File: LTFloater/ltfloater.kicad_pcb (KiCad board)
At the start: 2 copper layers, 97 parts, among them J1 USB_C_Receptacle, J2 USB_C_Receptacle, J3 TC2030-IDC, J4 D4, J5 D5, J6 A6, J7 A7, J8 B0, K0 K00, K1 K01, K10 K10, K11 K11, K12 K12, K13 K13, K14 K14, K14b1 K14, K2 K02, K20 K20, K21 K21, K22 K22, K23 K23, K24 K24, K3 K03, K30 K30, K31 K31, K31b1 K31, K32 K32, K33 K33, K34 K34, K34b1 K34, K4 K04, SW1 Switch-6P-2S2T, SW2 SW_Push, U1 MCP73831, U2 MCP1700 (3.0V), U3 MCP1700 (3.3V), U4 ATXMEGA-A4U-EPAD, U6 nRF24L01_module, U7 FSUSB42, U8 FSUSB42, U9 FSUSB42

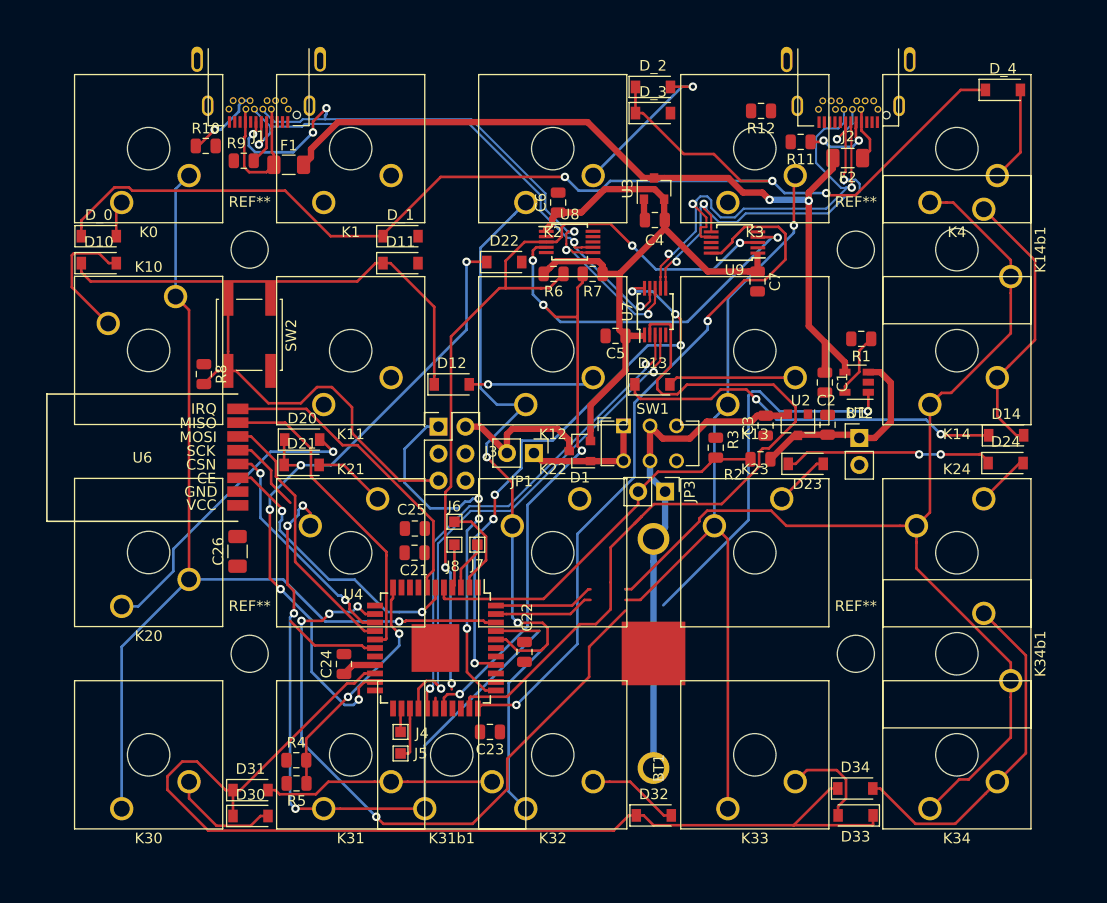
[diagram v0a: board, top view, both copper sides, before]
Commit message: Complete PCB, DRC violations limited to USB-C
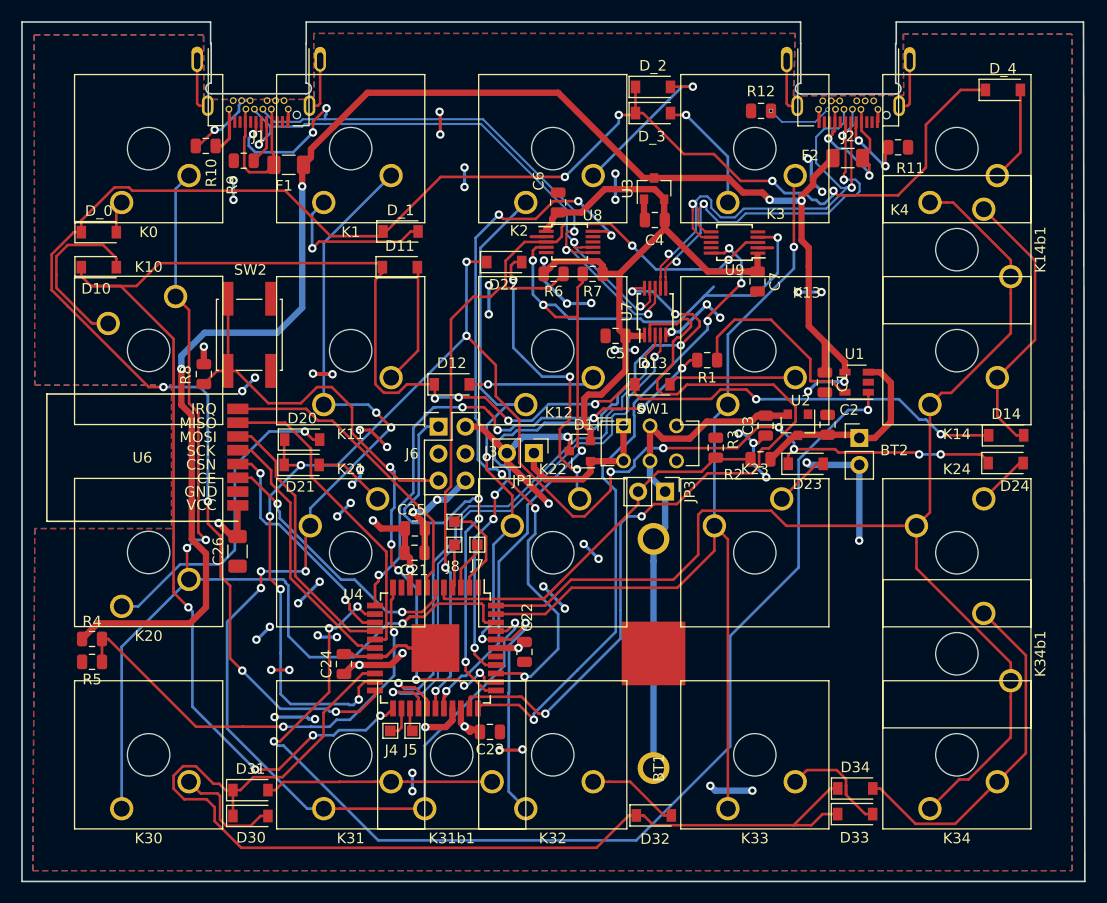
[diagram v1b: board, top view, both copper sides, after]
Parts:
- removed REF** (x4): MountingHole_3.5mm, MountingHole:MountingHole_3.5mm
- J1, J2: footprint Extra:USB_C_Receptacle_JAE_DX07B024XJ1 -> Extra:USB_C_Receptacle_JAE_DX07B024XJ1_cuts
- moved R5 22.4 mm to (98.2, 102.4)
- moved R4 22.4 mm to (98.2, 100.2)
- moved R1 14.7 mm to (156.2, 73.9)
- moved R11 9.21 mm to (174.2, 53.8), turned to 0 degrees
- moved J5 2.41 mm to (128.4, 108.9)
- moved J4 0.97 mm to (126.3, 108.9)
- moved D_1 0.44 mm to (127.3, 61.8)
- moved D11 0.39 mm to (127.2, 65.2)
- moved D_0 0.38 mm to (98.8, 61.8)
- moved D10 0.38 mm to (98.8, 65.2)
- moved D33 0.13 mm to (170.1, 116.7), turned to 0 degrees
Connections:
- U8 pad 10: Net-(U8-Pad10) -> /I2C_LEFT
- U8 pad 2: Net-(U8-Pad2) -> GND
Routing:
- net GND: track 2.00 -> 117.0 mm, vias 0 -> 52
- net /ROW1: track 80.8 -> 176.7 mm, vias 2 -> 10
- net /I2C_LEFT: track 0.00 -> 68.0 mm, vias 0 -> 6
- net +5V: track 78.2 -> 144.8 mm, vias 2 -> 4
- net /ROW0: track 115.9 -> 177.1 mm, vias 3 -> 8
- net /ROW2: track 84.2 -> 136.3 mm, vias 7 -> 12
- net /BAT_PROG: track 0.00 -> 50.9 mm, vias 0 -> 6
- net VCC: track 17.5 -> 63.4 mm, vias 0 -> 20
- net /COL1: track 69.5 -> 113.7 mm, vias 4 -> 6
- net /RST: track 36.4 -> 66.9 mm, vias 0 -> 6
- net Net-(D22-Pad2): track 0.00 -> 28.4 mm, vias 0 -> 3
- net /VBUS_CHECK: track 22.5 -> 43.6 mm
- net Net-(D_1-Pad2): track 0.00 -> 15.4 mm, vias 0 -> 1
- net Net-(R1-Pad1): track 6.06 -> 18.9 mm
- net Net-(D11-Pad2): track 0.00 -> 11.8 mm
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- added copper zone on F.Cu, net GND
- added copper zone on B.Cu, net VCC
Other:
- board outline added: 100.2 x 81 mm
- net class Fine added: clearance 0.15, trace_width 0.16, via_dia 0.4, via_drill 0.3
- net class Power: clearance 0.2 -> 0.15; trace_width 0.6 -> 0.3

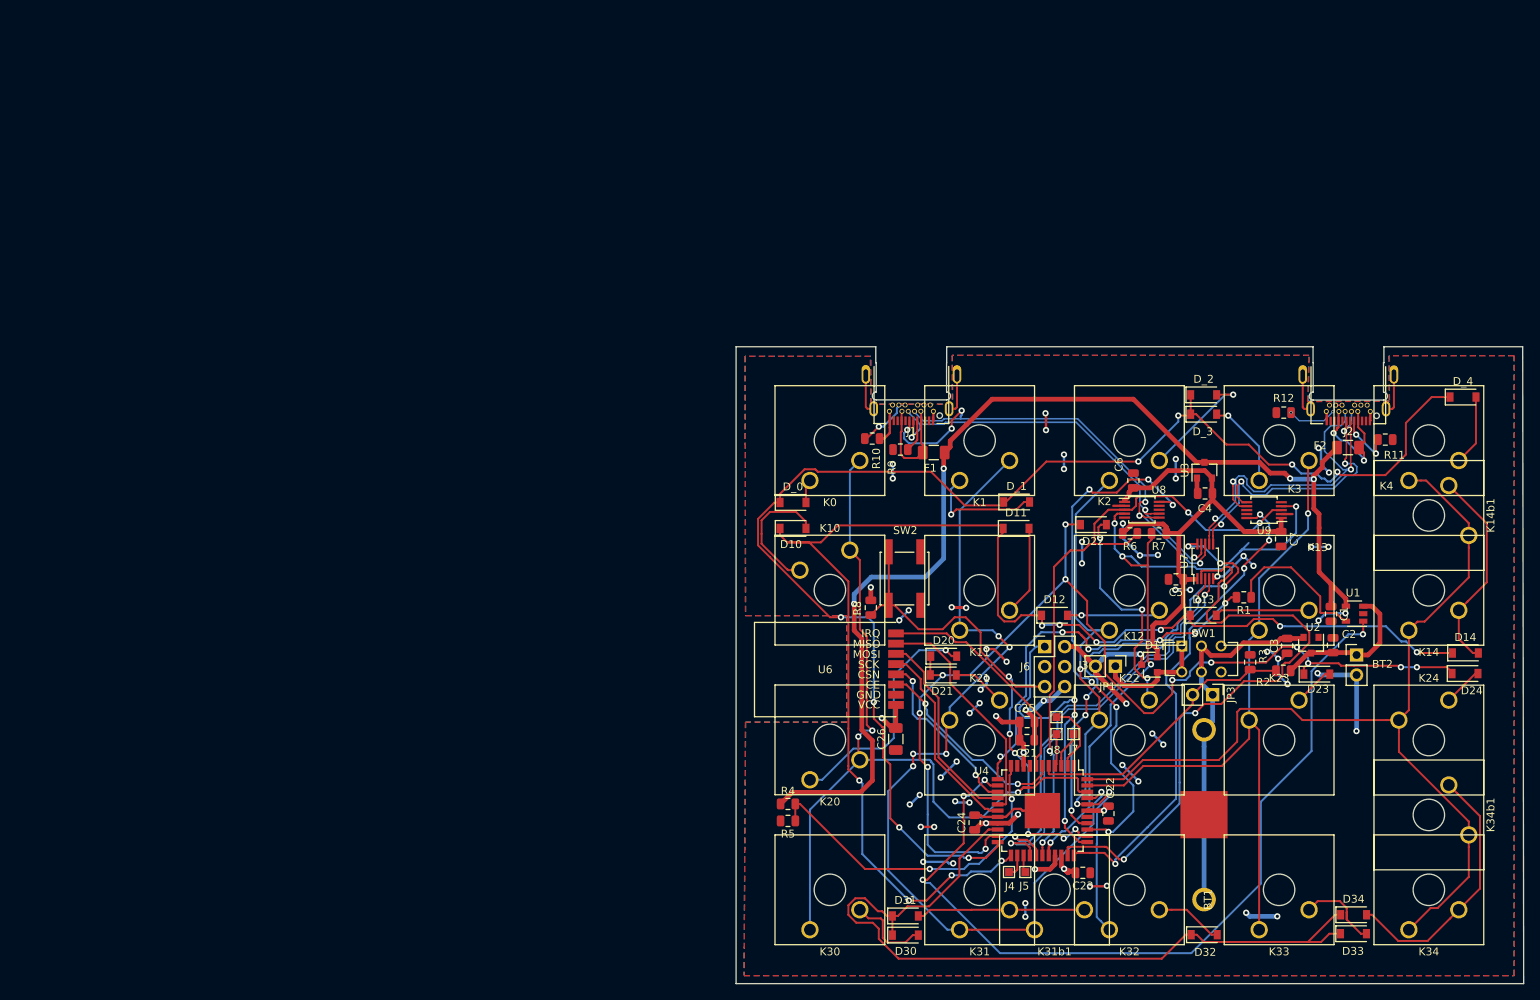
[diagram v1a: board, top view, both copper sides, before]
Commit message: Completely reworked PCB, with switches on the correct side, traces running mostly parrallel on a single side of the PCB
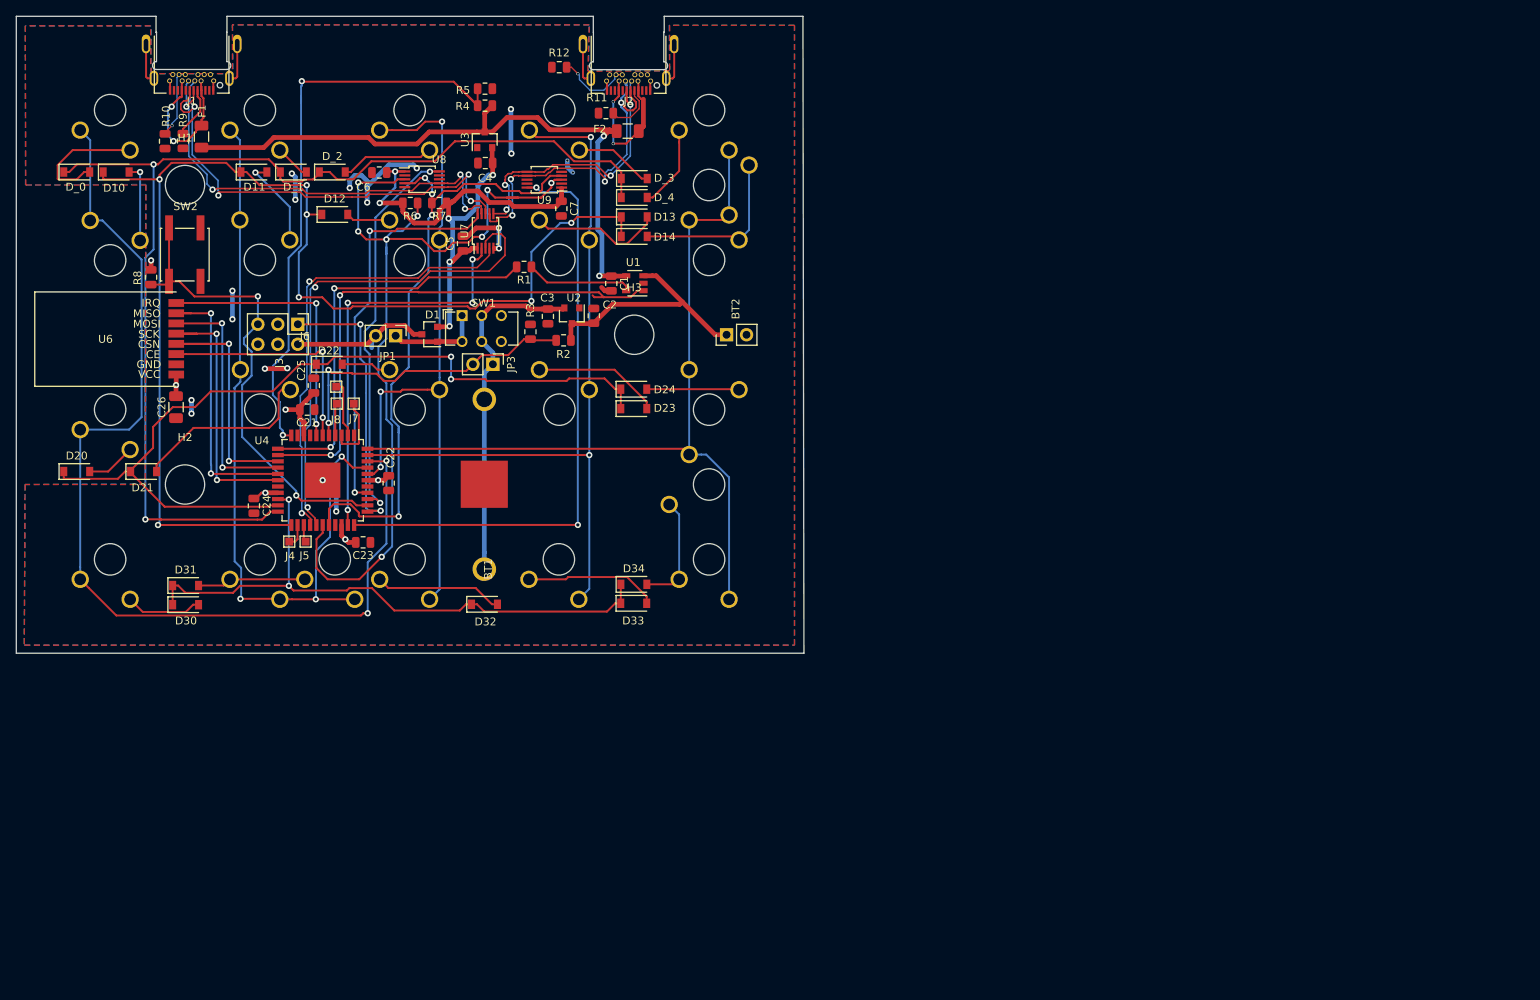
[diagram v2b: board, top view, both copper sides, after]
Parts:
- added H1: MountingHole, MountingHole:MountingHole_5mm, F.Cu at (21.5, 21.5)
- added H2: MountingHole, MountingHole:MountingHole_5mm, F.Cu at (21.5, 59.6)
- added H3: MountingHole, MountingHole:MountingHole_5mm, F.Cu at (78.6, 40.5)
- K0, K1, K10, K11, K12, K13, K14, K2, K20, K21, K22, K23, K24, K3, K30, K31, K31b1, K32, K33, K34, K4: moved to B.Cu
- K14b1: value K14 -> K13b; footprint Button_Switch_Keyboard:SW_Cherry_MX1A_2.00u_Plate -> Button_Switch_Keyboard:SW_Cherry_MX1A_1.00u_Plate; moved to B.Cu
- K34b1: value K34 -> K33b; footprint Button_Switch_Keyboard:SW_Cherry_MX1A_2.00u_Plate -> Button_Switch_Keyboard:SW_Cherry_MX1A_1.00u_Plate; moved to B.Cu
- moved D14 118.3 mm to (78.6, 28.0)
- moved D_2 114.4 mm to (40.2, 19.8)
- moved D20 112.8 mm to (7.68, 57.9)
- moved D24 111.8 mm to (78.6, 47.4)
- moved K34b1 110.1 mm to (83.1, 62.1)
- moved D_4 108.4 mm to (78.6, 23.1)
- moved R11 107.5 mm to (75.0, 12.3), turned to 180 degrees
- moved D11 107.0 mm to (30.2, 19.8)
- moved K11 105.4 mm to (28.4, 25.9)
- moved K12 105.4 mm to (47.5, 25.9)
- moved K13 105.4 mm to (66.5, 25.9)
- moved K14 105.4 mm to (85.6, 25.9)
- moved K22 105.4 mm to (47.5, 45.0), turned to 180 degrees
- moved K24 105.4 mm to (85.6, 45.0), turned to 180 degrees
- moved K23 105.4 mm to (66.5, 45.0), turned to 180 degrees
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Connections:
- K12 pad 1: /COL2 -> Net-(D12-Pad2)
- K12 pad 2: Net-(D12-Pad2) -> /COL2
- K13 pad 1: /COL3 -> Net-(D13-Pad2)
- K13 pad 2: Net-(D13-Pad2) -> /COL3
- K14b1 pad 1: /COL4 -> Net-(D14-Pad2)
- K14b1 pad 2: Net-(D14-Pad2) -> /COL4
- K2 pad 1: /COL2 -> Net-(D_2-Pad2)
- K2 pad 2: Net-(D_2-Pad2) -> /COL2
- K21 pad 1: Net-(D21-Pad2) -> /COL1
- K21 pad 2: /COL1 -> Net-(D21-Pad2)
- K24 pad 1: Net-(D24-Pad2) -> /COL4
- K24 pad 2: /COL4 -> Net-(D24-Pad2)
- K30 pad 1: /COL0 -> Net-(D30-Pad2)
- K30 pad 2: Net-(D30-Pad2) -> /COL0
- K34b1 pad 1: /COL4 -> Net-(D34-Pad2)
- K34b1 pad 2: Net-(D34-Pad2) -> /COL4
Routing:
- net GND: track 117.0 -> 49.8 mm, vias 52 -> 17
- net +5V: track 144.8 -> 83.4 mm, vias 4 -> 2
- net /BAT_STAT: track 109.0 -> 68.8 mm, vias 4 -> 2
- net /SDA: track 81.4 -> 116.4 mm, vias 4 -> 8
- net /VBUS_CHECK: track 43.6 -> 77.2 mm
- net /ROW0: track 177.1 -> 144.3 mm, vias 8 -> 2
- net /ROW2: track 136.3 -> 106.7 mm, vias 12 -> 2
- net /USB_SEL: track 80.1 -> 52.0 mm, vias 2 -> 4
- net /ROW3: track 103.2 -> 77.7 mm, vias 0 -> 2
- net /COL0: track 105.3 -> 129.6 mm, vias 3 -> 2
- net Net-(D20-Pad2): track 30.5 -> 6.30 mm, vias 1 -> 0
- net Net-(D22-Pad2): track 28.4 -> 6.32 mm, vias 3 -> 0
- net VCC: track 63.4 -> 43.7 mm, vias 20 -> 8
- net Net-(D34-Pad2): track 33.4 -> 14.4 mm
- net /I2C_LEFT: track 68.0 -> 50.1 mm, vias 6 -> 2
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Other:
- net class Power: trace_width 0.3 -> 0.6

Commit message: Now with 8 underglow LEDs on the PCB
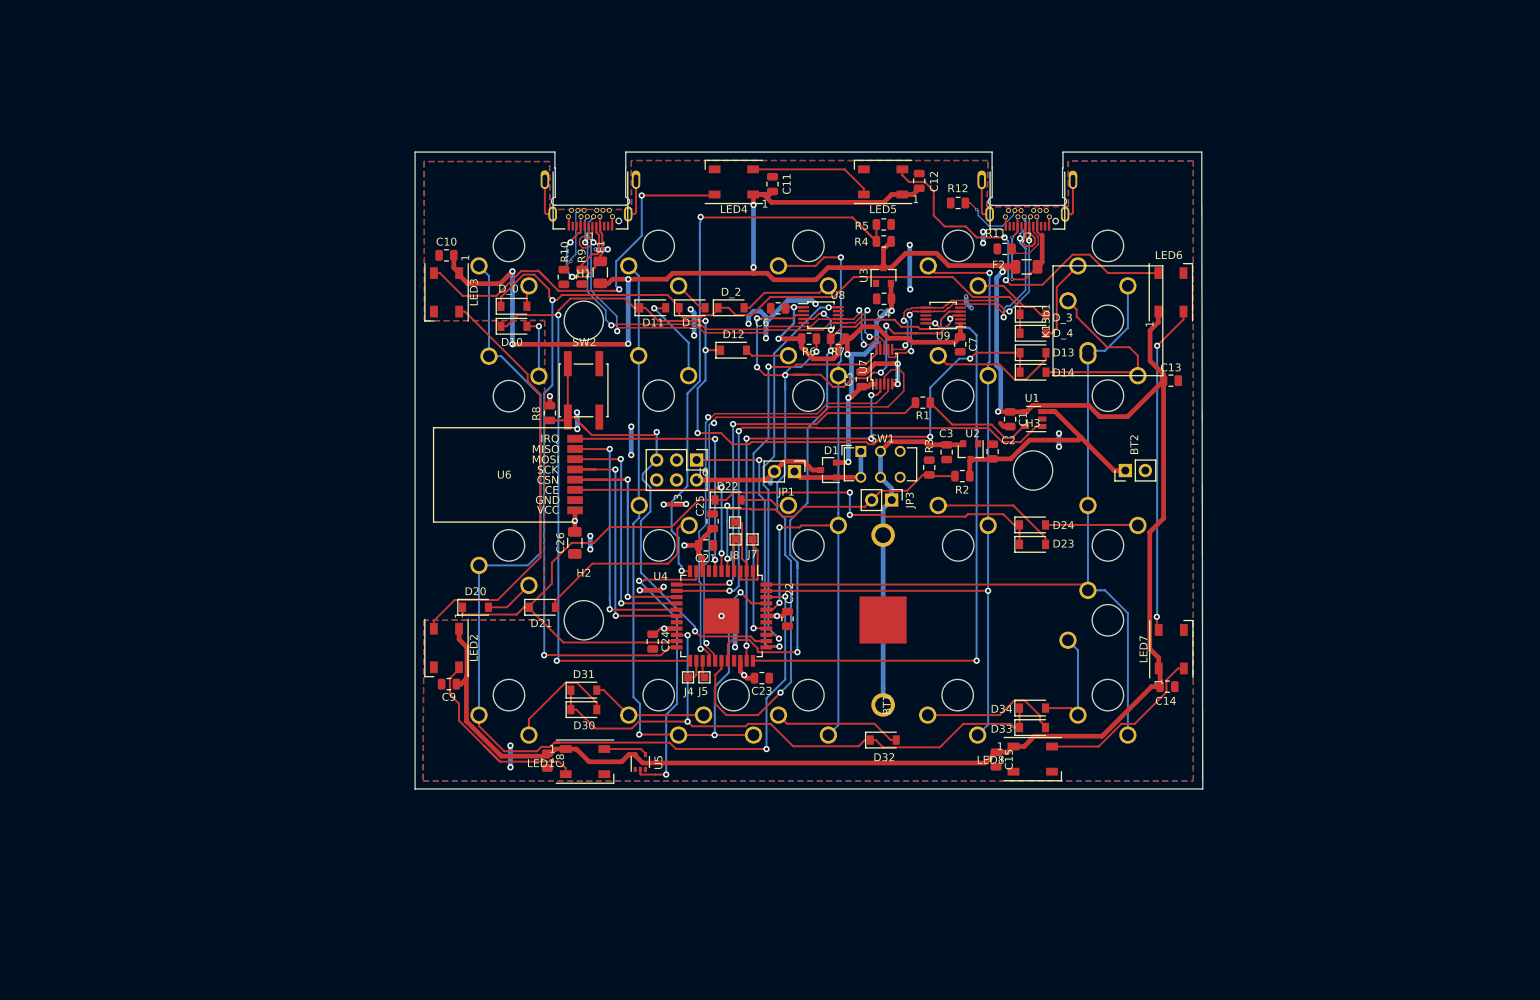
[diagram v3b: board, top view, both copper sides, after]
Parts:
- removed K14b1: K13b, Button_Switch_Keyboard:SW_Cherry_MX1A_1.00u_Plate
- added C10: 0.1uF, Capacitor_SMD:C_0805_2012Metric, F.Cu at (54.7, 30.4)
- added C11: 0.1uF, Capacitor_SMD:C_0805_2012Metric, F.Cu at (96.2, 21.4)
- added C12: 0.1uF, Capacitor_SMD:C_0805_2012Metric, F.Cu at (114.9, 20.9)
- added C13: 0.1uF, Capacitor_SMD:C_0805_2012Metric, F.Cu at (146.9, 46.4)
- added C14: 0.1uF, Capacitor_SMD:C_0805_2012Metric, F.Cu at (146.4, 85.3)
- added C15: 0.1uF, Capacitor_SMD:C_0805_2012Metric, F.Cu at (124.7, 94.6)
- added C8: 0.1uF, Capacitor_SMD:C_0805_2012Metric, F.Cu at (67.6, 94.7)
- added C9: 0.1uF, Capacitor_SMD:C_0805_2012Metric, F.Cu at (55.0, 85.0)
- added K13b1: K13b, Button_Switch_Keyboard:SW_Cherry_MX1A_2.00u_Plate, F.Cu at (133.8, 36.2)
- added LED1: WS2812B, LED_SMD:LED_WS2812B_PLCC4_5.0x5.0mm_P3.2mm, F.Cu at (72.4, 94.8)
- added LED2: WS2812B, LED_SMD:LED_WS2812B_PLCC4_5.0x5.0mm_P3.2mm, F.Cu at (54.7, 80.4)
- added LED3: WS2812B, LED_SMD:LED_WS2812B_PLCC4_5.0x5.0mm_P3.2mm, F.Cu at (54.7, 35.1)
- added LED4: WS2812B, LED_SMD:LED_WS2812B_PLCC4_5.0x5.0mm_P3.2mm, F.Cu at (91.3, 21.1)
- added LED5: WS2812B, LED_SMD:LED_WS2812B_PLCC4_5.0x5.0mm_P3.2mm, F.Cu at (110.3, 21.1)
- added LED6: WS2812B, LED_SMD:LED_WS2812B_PLCC4_5.0x5.0mm_P3.2mm, F.Cu at (146.9, 35.1)
- added LED7: WS2812B, LED_SMD:LED_WS2812B_PLCC4_5.0x5.0mm_P3.2mm, F.Cu at (146.9, 80.5)
- added LED8: WS2812B, LED_SMD:LED_WS2812B_PLCC4_5.0x5.0mm_P3.2mm, F.Cu at (129.3, 94.5)
- added U5: 74LVC1G34, Package_TO_SOT_SMD:SOT-353_SC-70-5, F.Cu at (79.4, 94.9)
- moved D_0 58.2 mm to (63.3, 36.9)
- moved D10 54.3 mm to (63.3, 39.4)
- moved BT1 53.6 mm to (110.3, 87.6)
- moved BT2 53.6 mm to (141.1, 57.8)
- moved C1 53.6 mm to (126.4, 51.3)
- moved C2 53.6 mm to (124.2, 55.4)
- moved C21 53.6 mm to (87.7, 67.3)
- moved C24 53.6 mm to (81.0, 79.6)
- moved C3 53.6 mm to (118.4, 55.5)
- moved C7 53.6 mm to (120.1, 41.7)
- moved D13 53.6 mm to (129.3, 42.8)
- moved D14 53.6 mm to (129.4, 45.3)
- moved D21 53.6 mm to (66.9, 75.2)
- moved D22 53.6 mm to (90.6, 61.5)
- moved D23 53.6 mm to (129.3, 67.2)
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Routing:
- net +5V: track 83.4 -> 341.9 mm, vias 2 -> 8
- net Net-(LED2-Pad2): track 0.00 -> 54.0 mm
- net Net-(LED3-Pad2): track 0.00 -> 52.4 mm, vias 0 -> 2
- net Net-(LED5-Pad2): track 0.00 -> 46.8 mm, vias 0 -> 2
- net Net-(LED6-Pad2): track 0.00 -> 42.0 mm, vias 0 -> 2
- net /UNDER_LED: track 0.00 -> 39.5 mm, vias 0 -> 2
- net Net-(LED1-Pad2): track 0.00 -> 27.2 mm
- net Net-(LED7-Pad2): track 0.00 -> 21.8 mm
- net Net-(LED4-Pad2): track 0.00 -> 15.9 mm
- net Net-(D_0-Pad2): track 16.2 -> 2.71 mm
- net GND: track 49.8 -> 59.3 mm, vias 17 -> 27
- net Net-(LED1-Pad4): track 0.00 -> 5.60 mm
- net Net-(D14-Pad2): track 21.9 -> 26.7 mm
- net Net-(D30-Pad2): track 9.76 -> 14.5 mm
- net VCC: track 43.7 -> 47.0 mm, vias 8 -> 10
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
